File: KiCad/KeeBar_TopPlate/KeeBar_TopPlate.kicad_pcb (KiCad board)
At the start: 2 copper layers, 376 x 86.5 mm, 68 parts, among them M2_1 Val**, M2_2 Val**, M2_3 Val**, M2_4 Val**, M2_5 Val**, M2_6 Val**, M2_7 Val**, M2_8 Val**, M2_9 Val**, SW1 SW_Push, SW10 SW_Push, SW11 SW_Push, SW12 SW_Push, SW13 SW_Push, SW14 SW_Push, SW15 SW_Push, SW16 SW_Push, SW17 SW_Push, SW18 SW_Push, SW19 SW_Push, SW2 SW_Push, SW20 SW_Push, SW21 SW_Push, SW22 SW_Push, SW23 SW_Push, SW24 SW_Push, SW25 SW_Push, SW26 SW_Push, SW27 SW_Push, SW28 SW_Push, SW29 SW_Push, SW3 SW_Push, SW30 SW_Push, SW31 SW_Push, SW32 SW_Push, SW33 SW_Push, SW34 SW_Push, SW35 SW_Push, SW36 SW_Push, SW37 SW_Push, SW38 SW_Push, SW39 SW_Push, SW4 SW_Push, SW40 SW_Push, SW41 SW_Push, SW42 SW_Push, SW43 SW_Push, SW44 SW_Push, SW45 SW_Push, SW46 SW_Push, SW47 SW_Push, SW48 SW_Push, SW49 SW_Push, SW5 SW_Push, SW50 SW_Push, SW51 SW_Push, SW53 SW_Push, SW55 SW_Push, SW56 SW_Push, SW57 SW_Push, SW58 SW_Push, SW59 SW_Push, SW6 SW_Push, SW60 SW_Push, SW7 SW_Push, SW8 SW_Push, SW9 SW_Push

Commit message: v1.1設計の更新
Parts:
- removed SW15: SW_Push, kbd_SW_Hole:SW_Hole_1.5u
- removed SW16, SW53: SW_Push, kbd_SW_Hole:SW_Hole_1u
- added ?: KEY_SWITCH, kbd_SW_Hole:SW_Hole_2u, F.Cu at (345.3, 71.4)
- added Omnispacebar: SW_JointHole_Omnispacebar, KeeBar-footprints:SW_JointHole_Omnispacebar, F.Cu at (190.6, 113.3)
- added REF**: , KeeBar-footprints:SW_JointHole_1u_1.5u, F.Cu at (342.9, 52.4)
- M2_1, M2_2, M2_3, M2_4, M2_5, M2_6, M2_7, M2_8, M2_9: footprint kbd_Hole:m2_Spacer_Hole_EdgeCuts -> kbd_Hole:m2_Spacer_Hole
- moved M2_3 25.0 mm to (287.0, 62.0)
- moved M2_8 23.7 mm to (287.0, 104.8)
- moved M2_4 16.2 mm to (361.5, 62.0)
- moved M2_9 12.2 mm to (361.5, 104.8)
- moved M2_5 5.83 mm to (205.0, 83.5)
- moved M2_7 3.34 mm to (117.0, 104.8)
- moved M2_1 2.50 mm to (50.0, 62.0)
- moved M2_2 2.50 mm to (117.0, 62.0)
- moved M2_6 2.30 mm to (50.0, 104.8)
- renumbered G*** to ?
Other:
- outline, holes or cut-outs redrawn
- board text added: "KeeBar v1.1 @ymkn"
- board text removed: "KeeBar Top Plate v1.0 @ymkn"
- board text removed: "SW52"
- board text removed: "SW54"

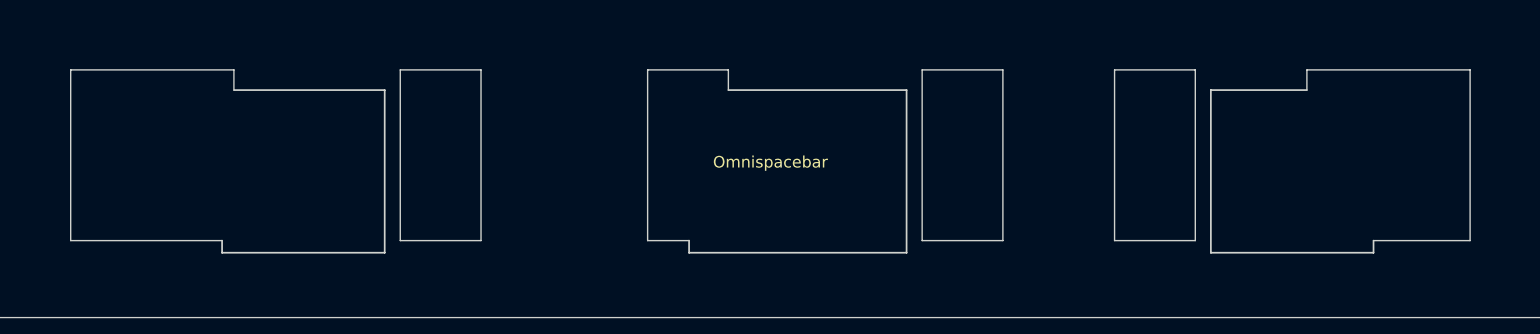
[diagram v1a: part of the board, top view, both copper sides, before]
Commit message: プレートのスペースバー位置がずれていたのを修正
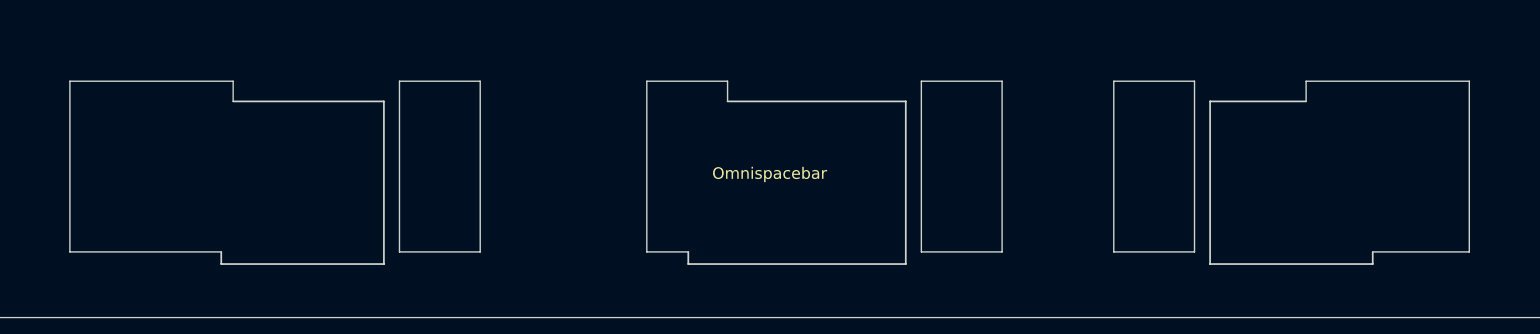
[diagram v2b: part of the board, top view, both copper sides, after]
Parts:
- moved Omnispacebar 0.98 mm to (190.5, 114.3)
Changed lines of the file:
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@@
   )
   (footprint "KeeBar-footprints:SW_JointHole_Omnispacebar" (layer "F.Cu")
-    (at 190.56875 113.31875)
+    (at 190.5 114.3)
     (attr through_hole)
     (fp_text reference "Omnispacebar" (at 0 -0.79 unlocked) (layer "F.SilkS")

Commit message: Enterに重なっていた不要なオブジェクトを削除
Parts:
- removed the ? at (345.3, 71.4)
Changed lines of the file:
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@@
-      (stroke (width 0.15) (type solid)) (layer "F.Fab"))
-  )
-  (footprint "kbd_SW_Hole:SW_Hole_2u" (layer "F.Cu")
-    (at 345.28125 71.4375)
-    (attr through_hole)
-    (fp_text reference "" (at 7 8.1) (layer "Edge.Cuts") hide
-        (effects (font (size 1 1) (thickness 0.15)))
-    )
-    (fp_text value "KEY_SWITCH" (at -7.4 -8.1) (layer "F.Fab") hide
-        (effects (font (size 1 1) (thickness 0.15)))
-    )
-    (fp_text user "${REFERENCE}" (at 0 0) (layer "F.Fab")
-        (effects (font (size 1 1) (thickness 0.15)))
-    )
-    (fp_line (start -15.4 -6) (end -8.4 -6)
-      (stroke (width 0.12) (type solid)) (layer "Edge.Cuts"))
-    (fp_line (start -15.4 8.8) (end -15.4 -6)
-      (stroke (width 0.12) (type solid)) (layer "Edge.Cuts"))
-    (fp_line (start -8.4 -6) (end -8.4 8.8)
-      (stroke (width 0.12) (type solid)) (layer "Edge.Cuts"))
-    (fp_line (start -8.4 8.8) (end -15.4 8.8)
-      (stroke (width 0.12) (type solid)) (layer "Edge.Cuts"))
-    (fp_line (start -7.05 -7.05) (end 7.05 -7.05)
-      (stroke (width 0.15) (type solid)) (layer "Edge.Cuts"))
-    (fp_line (start -7.05 7.05) (end -7.05 -7.05)
-      (stroke (width 0.15) (type solid)) (layer "Edge.Cuts"))
-    (fp_line (start 7.05 -7.05) (end 7.05 7.05)
-      (stroke (width 0.15) (type solid)) (layer "Edge.Cuts"))
-    (fp_line (start 7.05 7.05) (end -7.05 7.05)
-      (stroke (width 0.15) (type solid)) (layer "Edge.Cuts"))
-    (fp_line (start 8.4 -6) (end 8.4 8.8)
-      (stroke (width 0.12) (type solid)) (layer "Edge.Cuts"))
-    (fp_line (start 8.4 8.8) (end 15.4 8.8)
-      (stroke (width 0.12) (type solid)) (layer "Edge.Cuts"))
-    (fp_line (start 15.4 -6) (end 8.4 -6)
-      (stroke (width 0.12) (type solid)) (layer "Edge.Cuts"))
-    (fp_line (start 15.4 8.8) (end 15.4 -6)
-      (stroke (width 0.12) (type solid)) (layer "Edge.Cuts"))
-    (fp_line (start -19.05 -9.525) (end -19.05 9.525)
-      (stroke (width 0.15) (type solid)) (layer "F.Fab"))
-    (fp_line (start -19.05 9.525) (end 19.05 9.525)
-      (stroke (width 0.15) (type solid)) (layer "F.Fab"))
-    (fp_line (start 19.05 -9.525) (end -19.05 -9.525)
-      (stroke (width 0.15) (type solid)) (layer "F.Fab"))
-    (fp_line (start 19.05 9.525) (end 19.05 -9.525)
       (stroke (width 0.15) (type solid)) (layer "F.Fab"))
   )
@@
     (at 190.5 114.3)
     (attr through_hole)
-    (fp_text reference "Omnispacebar" (at 0 -0.79 unlocked) (layer "F.SilkS")
+    (fp_text reference "Omnispacebar" (at 0 -0.79 unlocked) (layer "F.SilkS") hide
         (effects (font (size 1 1) (thickness 0.1)))
     )
@@
   )
   (dimension (type aligned) (layer "Cmts.User")
-    (pts (xy 389.5 39.75) (xy 387 39.75))
-    (height 3.15)
-    (gr_text "2.5000 mm" (at 388.25 35.45) (layer "Cmts.User")
-      (effects (font (size 1 1) (thickness 0.15)))
-    )
-    (format (prefix "") (suffix "") (units 2) (units_format 1) (precision 4))
-    (style (thickness 0.15) (arrow_length 1.27) (text_position_mode 0) (extension_height 0.58642) (extension_offset 0.5) keep_text_aligned)
-  )
-  (dimension (type aligned) (layer "Cmts.User")
     (pts (xy 21.5 39.5) (xy 397.5 39.5))
     (height -20.3)
@@
   )
   (dimension (type aligned) (layer "Cmts.User")
-    (pts (xy 371.5 39.75) (xy 374 39.75))
-    (height -3.75)
-    (gr_text "2.5000 mm" (at 372.75 34.85) (layer "Cmts.User")
-      (effects (font (size 1 1) (thickness 0.15)))
-    )
-    (format (prefix "") (suffix "") (units 2) (units_format 1) (precision 4))
-    (style (thickness 0.15) (arrow_length 1.27) (text_position_mode 0) (extension_height 0.58642) (extension_offset 0.5) keep_text_aligned)
-  )
-  (dimension (type aligned) (layer "Cmts.User")
-    (pts (xy 389.5 40.3) (xy 397.5 40.3))
-    (height -5.4)
-    (gr_text "8.0000 mm" (at 393.5 33.75) (layer "Cmts.User")
-      (effects (font (size 1 1) (thickness 0.15)))
-    )
-    (format (prefix "") (suffix "") (units 2) (units_format 1) (precision 4))
-    (style (thickness 0.2) (arrow_length 1.27) (text_position_mode 0) (extension_height 0.58642) (extension_offset 0.5) keep_text_aligned)
-  )
-  (dimension (type aligned) (layer "Cmts.User")
     (pts (xy 361.5 59.5) (xy 21.5 59.5))
     (height 36.2)
@@
       (effects (font (size 1 1) (thickness 0.15)))
     )
-    (format (prefix "") (suffix "") (units 2) (units_format 1) (precision 4))
-    (style (thickness 0.15) (arrow_length 1.27) (text_position_mode 0) (extension_height 0.58642) (extension_offset 0.5) keep_text_aligned)
-  )
-  (dimension (type aligned) (layer "Cmts.User")
-    (pts (xy 387 39.8) (xy 374 39.8))
-    (height 2.3)
-    (gr_text "13.0000 mm" (at 380.5 36.35) (layer "Cmts.User")
-      (effects (font (size 1 1) (thickness 0.15)))
-    )
